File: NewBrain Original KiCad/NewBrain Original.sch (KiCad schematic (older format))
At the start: 18 parts, among them U410 MC1489N, U411 MC1488N, U426 74LS86, U436 74LS166, U437 74LS08, U438 74LS04, U440 74LS02, U447 74LS393, U453 2716-Memory_EPROM, U456 74LS32, U457 74LS10, U458 74LS90, U459 74LS32, U468 74LS393

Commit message: Add some more.
Signed-off-by: John Bradley <flypie@rocketmail.com>
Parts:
- added C? (x4): C, symbol Device:C
- added C?: CP, symbol Device:CP
- added J? (x2): Conn_02x03_Top_Bottom, symbol Connector_Generic:Conn_02x03_Top_Bottom
- added R74, R75: 2K, symbol Device:R_POT
- added R? (x12): R, symbol Device:R
- added U100: ZTX107, symbol Device:Q_NPN_EBC
- added U107, U109: IN914, symbol Device:D
- added U414: LM358, symbol Amplifier_Operational:LM358
- added U417, U439 (x2), U467: 74LS04, symbol 74xx:74LS04
- added U420: 74LS374, symbol 74xx:74LS374
- added U434: 74LS86, symbol 74xx:74LS86
- added U437: 74LS08, symbol 74xx:74LS08
- added unit 3 of U437
- added unit 2 of U438
- added U454: 74LS166, symbol 74xx:74LS166
- added U455: 74LS27, symbol 74xx:74LS27
- added U460: 74LS112, symbol 74xx:74LS112
- added U?: LM358, symbol 74xx:74LS112
- U438: value 74LS04 -> 74LS08
- U?: value 74LS393 -> LM358
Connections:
- net AB-0: now also U420.12 (O4), U454.14 (H), U455.11
- net AB-1: now also U420.15 (O5), U454.12 (G), U455.10
- net AB-2: now also U420.9 (O3), U454.11 (F), U455.9
- net AB-3: now also U420.6 (O2), U454.10 (E), U455.5
- net AB-4: now also U420.16 (O6), U454.5 (D), U455.4
- net AB-5: now also U420.19 (O7), U454.4 (C), U455.1
- net AB-6: now also U420.5 (O1), U454.3 (B), U455.13
- net AB-8: now also U437.6
- net GND: now also C?.1, J?.6 (Pin_6), J?.6 (Pin_6), R?.1, R?.1, R?.1, U100.1 (E), U109.1 (K), U420.1 (OE), U420.10 (GND), U454.1 (Ds), U454.6 (CE), U454.8 (GND)
- net GR: now also U454.9 (Clr)
- net LDSR: now also U460.13 (C)
- net TVSD: now also U437.9, U439.5
- net TXT: now also U437.2, U457.11, U455.12
- net VCC: now also R?.1, R?.2, U420.20 (VCC), U454.16 (VCC), U460.10 (~S)
- net ~CKVSR: now also U454.7 (Clk)
- net ~GR: now also U460.14 (~R)
- net ~LDVSR: now also U454.15 (PE)
- net at U457.10: now also U455.6
- net ~RSTFRM: now reaches U457.8
- net at U457.9: now also U455.8
- net RV: now reaches U426.1
- net at U426.2: now also U438.6
- net RVF: now reaches U426.3
- net at U437.4: now also U420.2 (O0), U437.10, U454.2 (A), U455.3
- net FS: now reaches U437.5
- net FS: now also U439.11
- new net: U438.4, U439.10
- new net: U437.8, U439.1, U460.11 (J)
- new net: U438.5, U460.9 (Q)
- new net: U439.2, U460.12 (K)
- new net: U414.1, U417.9
- new net: R?.1, R?.1, R?.2, U414.2 (-)
- new net: C?.1, R?.2 (x2)
- new net: U107.1 (K), U109.2 (A)
- new net: R?.1, R?.2, U107.2 (A)
- new net: C?.1, R?.1, U100.2 (B)
- new net: C?.2, C?.2, R?.1, U100.3 (C)
- new net: C?.1, R?.2, R?.2
- new net: R75.1, R?.1
- new net: R75.3, R?.2
- new net: R74.1, R?.1
- new net: R74.3, R?.2
- new net 1\2: U467.11
- new net BIAS: C?.2, R?.2, R?.2, U414.3 (+)
- new net IFT1: C?.2, J?.1 (Pin_1)
- new net IFT2: C?.2, J?.1 (Pin_1)
- new net OTT1: J?.2 (Pin_2), R75.2
- new net OTT2: J?.2 (Pin_2), R74.2
- new net RD0: U420.13 (D4)
- new net RD1: U420.14 (D5)
- new net RD2: U420.8 (D3)
- new net RD3: U420.7 (D2)
- new net RD4: U420.17 (D6)
- new net RD5: U420.18 (D7)
- new net RD6: U420.4 (D1)
- new net RD7: U420.3 (D0)
- new net SOGRSR: U454.13 (Qh)
- new net TDI: U434.8
- new net TDO: R?.2, U434.10
- new net TDTPLP0: J?.5 (Pin_5)
- new net TDTPLP1: J?.5 (Pin_5)
- new net TMS1: J?.3 (Pin_3)
- new net TMS2: J?.3 (Pin_3)
- new net TPIN: U417.8, U434.9
- new net ~TMS1: J?.4 (Pin_4)
- new net ~TMS2: J?.4 (Pin_4)
- new net ~TVCLK: U420.11 (Cp)
- new net ~TVSD: U439.6, U455.2
- no-connect marks 1 -> 2
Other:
- moved on the sheet: U426A, U437B, U447A, U447B, U457C, U468A, U468B

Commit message: First Drawing first draft.
Signed-off-by: John Bradley <flypie@rocketmail.com>
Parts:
- removed U437: 74LS08, symbol 74xx:74LS08
- removed unit 1 of U438
- removed U439: 74LS04, symbol 74xx:74LS04
- removed unit 1 of U440
- removed unit 3 of U440
- removed unit 1 of U459
- added C10, C6, C8, C9: C, symbol Device:C
- added C124: 150pf, symbol Device:C
- added C132: 680pf, symbol Device:C
- added C133, C73: 470pf, symbol Device:C
- added C7: CP, symbol Device:CP
- added C72: 220pf, symbol Device:C
- added L117: 47uH, symbol Device:L
- added Q1: Q_PNP_EBC, symbol Device:Q_PNP_EBC
- added R123, R13: 470, symbol Device:R
- added R131: 100, symbol Device:R
- added R14, R15, R16, R17, R18, R19, R20, R21, R22: R, symbol Device:R
- added U415: HE721A0530, HE721A0510, symbol SamacSys_Parts:HE721A0510
- added U416: HE751A0510, HE751A0510, symbol SamacSys_Parts:HE751A0510
- added U431, U433, U462, U463: 74LS32, symbol 74xx:74LS32
- added unit 4 of U434
- added unit 1 of U434
- added U435, U450: 74LS04, symbol 74xx:74LS04
- added unit 1 of U438
- added U441: 74LS32, symbol 74xx:74LS04
- added U446: 74LS21, symbol 74xx:74LS08
- added U448, U469: 74LS10, symbol 74xx:74LS10
- added U449: 74LS157, symbol 74xx:74LS157
- added U451: SN74LS279AN, DIP794W53P254L1930H508Q16N, symbol SamacSys_Parts:SN74LS279AN
- added U461: 74LS32, symbol 74xx:74LS95
- added U464: 74LS27, symbol 74xx:74LS27
- added U465, U471: 74LS11, symbol 74xx:74LS11
- added U466: 74LS21, symbol 74xx:74LS21
- added unit 4 of U467
- added unit 1 of U467
- added unit 3 of U467
- added unit 2 of U467
- added unit 6 of U467
- added U470: 74LS00, symbol 74xx:74LS00
- U1, U2: renamed from U?; value LM358 -> 74LS21
- U438: symbol 74xx:74LS04 -> 74xx:74LS08
- U439: renamed from U438; value 74LS08 -> 74LS04
- gave numbers to parts that had none: 21
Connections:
- net labels added: 1\8, BUSRQ, CMPVID, CMSNC, CSYNC, FP, FPO, FRM, HSYNC, K11, K12, LLVD, TVP, ~32, ~BUSRQ, ~CLCLK, ~CLKINT, ~FRM, ~FRMR, ~TM1, ~TM2, ~TVS
- wire segments 299 -> 654
- no-connect marks 2 -> 3
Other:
- moved on the sheet: J3, J4, U2E, U426E, U437E, U440E, U453B, U455D, U456A, U456C, U456D, U456E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

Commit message: Start sheet TWO.
Signed-off-by: John Bradley <flypie@rocketmail.com>
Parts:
- removed C1, C7: CP, symbol Device:CP
- removed C10, C2, C3, C4, C5, C6, C8, C9: C, symbol Device:C
- removed C124: 150pf, symbol Device:C
- removed C132: 680pf, symbol Device:C
- removed C133, C73: 470pf, symbol Device:C
- removed C72: 220pf, symbol Device:C
- removed J1, J2, J3, J4: Conn_02x03_Top_Bottom, symbol Connector_Generic:Conn_02x03_Top_Bottom
- removed L117: 47uH, symbol Device:L
- removed Q1: Q_PNP_EBC, symbol Device:Q_PNP_EBC
- removed R1, R10, R11, R12, R14, R15, R16, R17, R18, R19, R2, R20, R21, R22, R3, R4, R5, R6, R7, R8, R9: R, symbol Device:R
- removed R123, R13: 470, symbol Device:R
- removed R131: 100, symbol Device:R
- removed R61: 22K, symbol Device:R
- removed R74, R75: 2K, symbol Device:R_POT
- removed U100: ZTX107, symbol Device:Q_NPN_EBC
- removed U107, U109: IN914, symbol Device:D
- removed U410: MC1489N, DIP794W53P254L1930H508Q14N, symbol SamacSys_Parts:MC1489N
- removed U411: MC1488N, DIP794W53P254L1930H508Q14N, symbol SamacSys_Parts:MC1488N
- removed U414: LM358, symbol Amplifier_Operational:LM358
- removed U415: HE721A0530, HE721A0510, symbol SamacSys_Parts:HE721A0510
- removed U416: HE751A0510, HE751A0510, symbol SamacSys_Parts:HE751A0510
- removed U417, U435, U439, U450, U467: 74LS04, symbol 74xx:74LS04
- removed U420: 74LS374, symbol 74xx:74LS374
- removed unit 1 of U426
- removed unit 2 of U426
- removed U431, U433, U459, U462, U463: 74LS32, symbol 74xx:74LS32
- removed U434: 74LS86, symbol 74xx:74LS86
- removed U436, U454: 74LS166, symbol 74xx:74LS166
- removed unit 1 of U437
- removed unit 2 of U437
- removed unit 4 of U437
- removed unit 3 of U437
- removed unit 2 of U438
- removed unit 1 of U438
- removed unit 4 of U440
- removed unit 2 of U440
- removed U441: 74LS32, symbol 74xx:74LS04
- removed U446: 74LS21, symbol 74xx:74LS08
- removed U447, U468: 74LS393, symbol 74xx:74LS393
- removed U448, U469: 74LS10, symbol 74xx:74LS10
- removed U449: 74LS157, symbol 74xx:74LS157
- removed unit 2 of U451
- removed unit 3 of U451
- removed unit 4 of U451
- removed unit 1 of U451
- removed unit 1 of U453
- removed unit 3 of U455
- removed unit 2 of U455
- removed unit 1 of U455
- removed unit 1 of U456
- removed unit 4 of U456
- removed unit 2 of U456
- removed unit 3 of U456
- removed unit 2 of U457
- removed unit 3 of U457
- removed unit 1 of U457
- removed U458: 74LS90, symbol 74xx:74LS90
- removed U460: 74LS112, symbol 74xx:74LS112
- removed U461: 74LS32, symbol 74xx:74LS95
- removed U464: 74LS27, symbol 74xx:74LS27
- removed U465, U471: 74LS11, symbol 74xx:74LS11
- removed U466: 74LS21, symbol 74xx:74LS21
- removed U470: 74LS00, symbol 74xx:74LS00
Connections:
- net labels removed: 1\2, 1\4, 1\8, AB-0, AB-1, AB-10, AB-2, AB-3, AB-4, AB-5, AB-6, AB-7, AB-8, AB-9, BIAS, BOL, BUSRQ, CMPVID, CMSNC, CRDO, CSYNC, DA-0, DA-1, DA-2, DA-3, DA-4, DA-5, DA-6, DA-7, DO, FP, FPO, FRM, FS, GR, HSYNC, IFT1, IFT2, K11, K12, LDSR, LLVD, OTT1, OTT2, PO, RC0, RC1, RC2, RC3, RD0, RD1, RD2, RD3, RD4, RD5, RD6, RD7, RDDK, RV, RVF, SOGRSR, SOVSR, TDI, TDO, TDTPLP0, TDTPLP1, TMS1, TMS2, TPIN, TVP, TVSD, TXT, TXTQ, UCR, ~1\2, ~32, ~BUSRQ, ~CKVSR, ~CLCLK, ~CLKINT, ~CTSD, ~CTSP, ~FRM, ~FRMR, ~GR, ~LDVSR, ~RSTFRM, ~RTSD, ~TM1, ~TM2, ~TMS1, ~TMS2, ~TVCLK, ~TVS, ~TVSD, ~VDLD
- wire segments 654 -> 22
- no-connect marks 3 -> 0
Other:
- moved on the sheet: U1A, U2E, U426E, U437E, U438E, U440E, U451E, U453B, U455D, U456E, U457D

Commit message: Complete most of drawing 2.
Signed-off-by: John Bradley <flypie@rocketmail.com>
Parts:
- removed U1: 74LS21, symbol 74xx:74LS112
- added U401: LM358, Package_DIP:DIP-8_W7.62mm, symbol Amplifier_Operational:LM358
- added U417: MC14584BDG, Package_DIP:DIP-14_W7.62mm, symbol SamacSys_Parts:MC14584BDG_UNITS
- added U418, U441, U470: 74LS00, Package_DIP:DIP-14_W7.62mm, symbol 74xx:74LS00
- added U425: 74LS74, Package_DIP:DIP-14_W7.62mm, symbol 74xx:74LS74
- added U429: 74LS139, Package_DIP:DIP-16_W7.62mm, symbol 74xx:74LS139
- added U431, U433, U459, U462, U463: 74LS32, Package_DIP:DIP-14_W7.62mm, symbol 74xx:74LS32
- added U432, U439, U450, U467: 74LS04, Package_DIP:DIP-14_W7.62mm, symbol 74xx:74LS04
- added U434: 74LS86, Package_DIP:DIP-14_W7.62mm, symbol 74xx:74LS86
- added U435: 74LS06, Package_DIP:DIP-14_W7.62mm, symbol 74xx:74LS06
- added U443, U464, U471: 74LS11, Package_DIP:DIP-14_W7.62mm, symbol 74xx:74LS11
- added U444: 74LS157_UNITS, Package_DIP:DIP-16_W7.62mm, symbol 74xx:74LS157_UNITS
- added U445, U460: 74LS112, Package_DIP:DIP-16_W7.62mm, symbol 74xx:74LS112
- added U446: 74LS21, Package_DIP:DIP-14_W7.62mm, symbol 74xx:74LS08
- added U447, U468: 74LS393, Package_DIP:DIP-14_W7.62mm, symbol 74xx:74LS393
- added U448, U469: 74LS10, Package_DIP:DIP-14_W7.62mm, symbol 74xx:74LS10
- added U449: 74LS157, Package_DIP:DIP-16_W7.62mm, symbol 74xx:74LS157_UNITS
- added U452: MC14584BDG_UNITS, Package_DIP:DIP-14_W7.62mm, symbol SamacSys_Parts:MC14584BDG_UNITS
- added U465: 74LS11, Package_DIP:DIP-14_W7.62mm, symbol 74xx:74LS27
- U426, U437, U438, U440, U455, U456, U457: footprint (none) -> Package_DIP:DIP-14_W7.62mm
- U451: footprint DIP794W53P254L1930H508Q16N -> Package_DIP:DIP-16_W7.62mm
- U466: renamed from U2; footprint (none) -> Package_DIP:DIP-14_W7.62mm; symbol 74xx:74LS32 -> 74xx:74LS21
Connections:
- wire segments 22 -> 101
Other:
- moved on the sheet: U426E, U437E, U440E, U451E, U453B, U455D, U456E, U457D

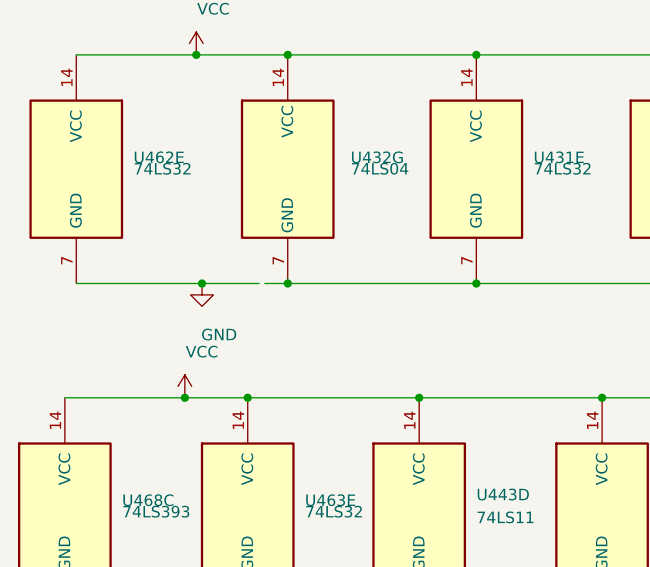
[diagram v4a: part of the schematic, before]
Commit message: Some more link fixes now below 100 warnings.
Signed-off-by: John Bradley <flypie@rocketmail.com>
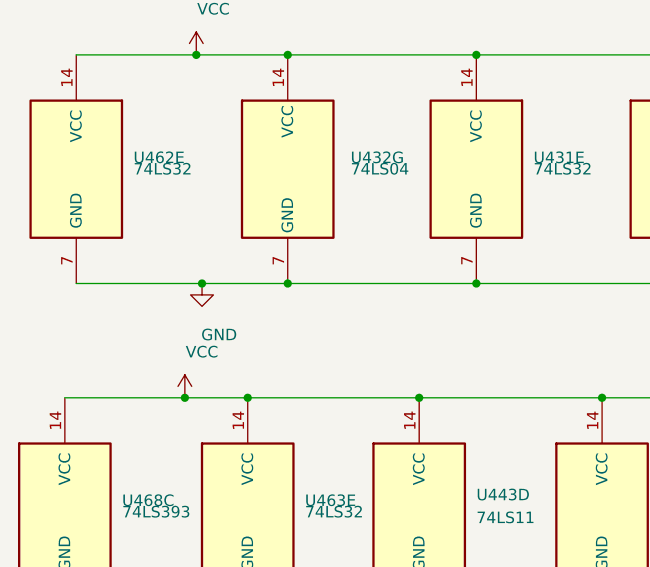
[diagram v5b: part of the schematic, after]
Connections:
- wire segments 101 -> 100
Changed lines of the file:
@@
 $EndComp
-Wire Wire Line
-	2050 12250 1800 12250
 Wire Wire Line
 	1250 11250 1775 11250
@@
 Wire Wire Line
 	1775 11250 2175 11250
-Wire Wire Line
-	2075 12250 2175 12250
 $Comp
 L 74xx:74LS32 U?
@@
 Wire Wire Line
 	6400 12250 10925 12250
+Wire Wire Line
+	1800 12250 2175 12250
 $EndSCHEMATC

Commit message: More Label fixing. Down to 16 Warnings. Lots of devie Labels and balues wrong.
Signed-off-by: John Bradley <flypie@rocketmail.com>
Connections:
- wire segments 100 -> 98
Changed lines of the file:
@@
 $EndComp
 Connection ~ 1775 15325
-Wire Wire Line
-	1775 15325 1500 15325
-$Comp
-L power:PWR_FLAG #FLG0102
-U 1 1 63B4C2B0
-P 1500 15325
-F 0 "#FLG0102" H 1500 15400 50  0001 C CNN
-F 1 "PWR_FLAG" H 1475 15525 50  0000 C CNN
-F 2 "" H 1500 15325 50  0001 C CNN
-F 3 "~" H 1500 15325 50  0001 C CNN
-	1    1500 15325
-	-1   0    0    1
-$EndComp
-Connection ~ 1500 15325
-Wire Wire Line
-	1500 15325 1225 15325
 $Sheet
 S 1250 2925 1500 1000
@@
 F1 "One.sch" 197
 $EndSheet
-Wire Wire Line
-	1450 14325 1225 14325
-Connection ~ 1450 14325
-$Comp
-L power:PWR_FLAG #FLG0101
-U 1 1 63B4BC3E
-P 1450 14325
-F 0 "#FLG0101" H 1450 14400 50  0001 C CNN
-F 1 "PWR_FLAG" H 1450 14525 50  0000 C CNN
-F 2 "" H 1450 14325 50  0001 C CNN
-F 3 "~" H 1450 14325 50  0001 C CNN
-	1    1450 14325
-	1    0    0    -1
-$EndComp
-Wire Wire Line
-	1750 14325 1450 14325
 Connection ~ 1750 14325
 $Comp
@@
 Wire Wire Line
 	1800 12250 2175 12250
+Wire Wire Line
+	1225 15325 1775 15325
+Wire Wire Line
+	1225 14325 1750 14325
 $EndSCHEMATC

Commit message: Resolve inconsistencies in circuit diagram buy following traces.
Resistor name used twice temp solution add a and b to name.

Signed-off-by: John Bradley <flypie@rocketmail.com>
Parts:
- removed U401: LM358, Package_DIP:DIP-8_W7.62mm, symbol Amplifier_Operational:LM358
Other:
- moved on the sheet: U429C, U439G, U441E, U450G
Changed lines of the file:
@@
 Connection ~ 2000 12750
-Wire Wire Line
-	2025 13750 2750 13750
 Wire Wire Line
 	18350 13750 18350 13900
@@
 $EndComp
 Connection ~ 10050 12750
-Wire Wire Line
-	10050 12750 10875 12750
 Connection ~ 10050 13750
-Wire Wire Line
-	10050 13750 10875 13750
 $Comp
 L 74xx:74LS04 U?
 U 7 1 6635F851
-P 10875 13250
+P 10850 13250
 AR Path="/648118A5/6635F851" Ref="U?"  Part="1"
 AR Path="/6635F851" Ref="U439"  Part="7"
-F 0 "U439" H 10600 13300 50  0000 R CNN
-F 1 "74LS04" H 10600 13250 50  0000 R CNN
-F 2 "Package_DIP:DIP-14_W7.62mm" H 10875 13250 50  0001 C CNN
-F 3 "http://www.ti.com/lit/gpn/sn74LS04" H 10875 13250 50  0001 C CNN
-	7    10875 13250
-	-1   0    0    -1
-$EndComp
-Connection ~ 10875 12750
-Wire Wire Line
-	10875 12750 11675 12750
-Connection ~ 10875 13750
-Wire Wire Line
-	10875 13750 11675 13750
+F 0 "U439" H 10575 13300 50  0000 R CNN
+F 1 "74LS04" H 10575 13250 50  0000 R CNN
+F 2 "Package_DIP:DIP-14_W7.62mm" H 10850 13250 50  0001 C CNN
+F 3 "http://www.ti.com/lit/gpn/sn74LS04" H 10850 13250 50  0001 C CNN
+	7    10850 13250
+	-1   0    0    -1
+$EndComp
 $Comp
 L 74xx:74LS08 U?
@@
 $EndComp
 Connection ~ 14075 12750
-Wire Wire Line
-	14075 12750 14925 12750
 Connection ~ 14075 13750
-Wire Wire Line
-	14075 13750 14925 13750
 $Comp
 L 74xx:74LS04 U?
 U 7 1 663B0DEC
-P 14925 13250
+P 14950 13250
 AR Path="/6480994A/663B0DEC" Ref="U?"  Part="5"
 AR Path="/663B0DEC" Ref="U450"  Part="7"
-F 0 "U450" H 15200 13300 50  0000 L CNN
-F 1 "74LS04" H 15200 13250 50  0000 L CNN
-F 2 "Package_DIP:DIP-14_W7.62mm" H 14925 13250 50  0001 C CNN
-F 3 "http://www.ti.com/lit/gpn/sn74LS04" H 14925 13250 50  0001 C CNN
-	7    14925 13250
-	1    0    0    -1
-$EndComp
-Connection ~ 14925 12750
-Wire Wire Line
-	14925 12750 15725 12750
-Connection ~ 14925 13750
-Wire Wire Line
-	14925 13750 15725 13750
+F 0 "U450" H 15225 13300 50  0000 L CNN
+F 1 "74LS04" H 15225 13250 50  0000 L CNN
+F 2 "Package_DIP:DIP-14_W7.62mm" H 14950 13250 50  0001 C CNN
+F 3 "http://www.ti.com/lit/gpn/sn74LS04" H 14950 13250 50  0001 C CNN
+	7    14950 13250
+	1    0    0    -1
+$EndComp
 $Comp
 L 74xx:74LS04 U?
@@
 $EndComp
 Connection ~ 15725 12750
-Wire Wire Line
-	15725 12750 16500 12750
 Connection ~ 15725 13750
-Wire Wire Line
-	15725 13750 16500 13750
 $Comp
 L 74xx:74LS00 U?
 U 5 1 663CC9E6
-P 16500 13250
+P 16550 13250
 AR Path="/648118A5/663CC9E6" Ref="U?"  Part="4"
 AR Path="/663CC9E6" Ref="U441"  Part="5"
-F 0 "U441" H 16750 13300 50  0000 L CNN
-F 1 "74LS00" H 16750 13250 50  0000 L CNN
-F 2 "Package_DIP:DIP-14_W7.62mm" H 16500 13250 50  0001 C CNN
-F 3 "http://www.ti.com/lit/gpn/sn74LS11" H 16500 13250 50  0001 C CNN
-	5    16500 13250
-	1    0    0    -1
-$EndComp
-Connection ~ 16500 12750
-Wire Wire Line
-	16500 12750 18350 12750
-Connection ~ 16500 13750
-Wire Wire Line
-	16500 13750 18350 13750
+F 0 "U441" H 16800 13300 50  0000 L CNN
+F 1 "74LS00" H 16800 13250 50  0000 L CNN
+F 2 "Package_DIP:DIP-14_W7.62mm" H 16550 13250 50  0001 C CNN
+F 3 "http://www.ti.com/lit/gpn/sn74LS11" H 16550 13250 50  0001 C CNN
+	5    16550 13250
+	1    0    0    -1
+$EndComp
 $Comp
 L power:GND #PWR0232
@@
 	5625 11250 6400 11250
 Connection ~ 5625 12250
-Wire Wire Line
-	5225 12750 6075 12750
-Wire Wire Line
-	5225 13750 6075 13750
 $Comp
 L 74xx:74LS139 U?
 U 3 1 6657C34F
-P 6075 13250
+P 6100 13250
 AR Path="/648118A5/6657C34F" Ref="U?"  Part="1"
 AR Path="/6657C34F" Ref="U429"  Part="3"
-F 0 "U429" H 5825 13325 50  0000 R CNN
-F 1 "74LS139" H 5825 13225 50  0000 R CNN
-F 2 "Package_DIP:DIP-16_W7.62mm" H 6075 13250 50  0001 C CNN
-F 3 "http://www.ti.com/lit/gpn/sn74LS04" H 6075 13250 50  0001 C CNN
-	3    6075 13250
-	-1   0    0    -1
-$EndComp
-Connection ~ 6075 12750
-Wire Wire Line
-	6075 12750 6875 12750
-Connection ~ 6075 13750
-Wire Wire Line
-	6075 13750 6875 13750
+F 0 "U429" H 5850 13325 50  0000 R CNN
+F 1 "74LS139" H 5850 13225 50  0000 R CNN
+F 2 "Package_DIP:DIP-16_W7.62mm" H 6100 13250 50  0001 C CNN
+F 3 "http://www.ti.com/lit/gpn/sn74LS04" H 6100 13250 50  0001 C CNN
+	3    6100 13250
+	-1   0    0    -1
+$EndComp
 $Comp
 L 74xx:74LS112 U?
@@
 	1    0    0    -1
 $EndComp
-$Comp
-L Amplifier_Operational:LM358 U?
-U 3 1 666BFD9E
-P 6500 11725
-AR Path="/648118A5/666BFD9E" Ref="U?"  Part="3"
-AR Path="/666BFD9E" Ref="U401"  Part="3"
-F 0 "U401" H 6500 11800 50  0000 L CNN
-F 1 "LM358" H 6500 11700 50  0000 L CNN
-F 2 "Package_DIP:DIP-8_W7.62mm" H 6500 11725 50  0001 C CNN
-F 3 "http://www.ti.com/lit/ds/symlink/lm2904-n.pdf" H 6500 11725 50  0001 C CNN
-	3    6500 11725
-	1    0    0    -1
-$EndComp
 Wire Wire Line
 	6400 11425 6400 11250
@@
 Wire Wire Line
 	1225 14325 1750 14325
+Wire Wire Line
+	10050 12750 10850 12750
+Wire Wire Line
+	10050 13750 10850 13750
+Connection ~ 10850 12750
+Wire Wire Line
+	10850 12750 11675 12750
+Connection ~ 10850 13750
+Wire Wire Line
+	10850 13750 11675 13750
+Wire Wire Line
+	5225 13750 6100 13750
+Wire Wire Line
+	5225 12750 6100 12750
+Connection ~ 6100 12750
+Wire Wire Line
+	6100 12750 6875 12750
+Connection ~ 6100 13750
+Wire Wire Line
+	6100 13750 6875 13750
+Wire Wire Line
+	15725 13750 16550 13750
+Wire Wire Line
+	15725 12750 16550 12750
+Connection ~ 16550 12750
+Wire Wire Line
+	16550 12750 18350 12750
+Connection ~ 16550 13750
+Wire Wire Line
+	16550 13750 18350 13750
+Wire Wire Line
+	14075 13750 14950 13750
+Wire Wire Line
+	14075 12750 14950 12750
+Connection ~ 14950 12750
+Wire Wire Line
+	14950 12750 15725 12750
+Connection ~ 14950 13750
+Wire Wire Line
+	14950 13750 15725 13750
+Wire Wire Line
+	2000 13750 2750 13750
+Connection ~ 2000 13750
 $EndSCHEMATC
